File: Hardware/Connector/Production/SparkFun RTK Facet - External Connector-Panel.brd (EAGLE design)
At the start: 231.2 x 149 mm, 826 parts, among them J1 FPC_12_0.5MM_BACKFLIP, J103 FPC_12_0.5MM_BACKFLIP, J104 FPC_12_0.5MM_BACKFLIP, J105 Qwiic, J106 u-blox USB, J111 FPC_12_0.5MM_BACKFLIP, J112 FPC_12_0.5MM_BACKFLIP, J113 Qwiic, J114 u-blox USB, J119 FPC_12_0.5MM_BACKFLIP, J120 FPC_12_0.5MM_BACKFLIP, J121 Qwiic, J122 u-blox USB, J127 FPC_12_0.5MM_BACKFLIP, J128 FPC_12_0.5MM_BACKFLIP, J129 Qwiic, J130 u-blox USB, J135 FPC_12_0.5MM_BACKFLIP, J136 FPC_12_0.5MM_BACKFLIP, J137 Qwiic, J138 u-blox USB, J143 FPC_12_0.5MM_BACKFLIP, J144 FPC_12_0.5MM_BACKFLIP, J145 Qwiic, J146 u-blox USB, J15 FPC_12_0.5MM_BACKFLIP, J151 FPC_12_0.5MM_BACKFLIP, J152 FPC_12_0.5MM_BACKFLIP, J153 Qwiic, J154 u-blox USB, J159 FPC_12_0.5MM_BACKFLIP, J16 FPC_12_0.5MM_BACKFLIP, J160 FPC_12_0.5MM_BACKFLIP, J17 Qwiic, J18 u-blox USB, J23 FPC_12_0.5MM_BACKFLIP, J24 FPC_12_0.5MM_BACKFLIP, J25 Qwiic, J26 u-blox USB, J3 Qwiic, J31 FPC_12_0.5MM_BACKFLIP, J32 FPC_12_0.5MM_BACKFLIP, J33 Qwiic, J34 u-blox USB, J39 FPC_12_0.5MM_BACKFLIP, J4 Qwiic, J40 FPC_12_0.5MM_BACKFLIP, J41 Qwiic, J42 u-blox USB, J47 FPC_12_0.5MM_BACKFLIP, J48 FPC_12_0.5MM_BACKFLIP, J49 Qwiic, J5 u-blox USB, J50 u-blox USB, J55 FPC_12_0.5MM_BACKFLIP, J56 FPC_12_0.5MM_BACKFLIP, J57 Qwiic, J58 u-blox USB, J6 FPC_12_0.5MM_BACKFLIP, J63 FPC_12_0.5MM_BACKFLIP, J64 FPC_12_0.5MM_BACKFLIP, J65 Qwiic, J66 u-blox USB, J7 u-blox USB, J71 FPC_12_0.5MM_BACKFLIP, J72 FPC_12_0.5MM_BACKFLIP, J73 Qwiic, J74 u-blox USB, J79 FPC_12_0.5MM_BACKFLIP, J80 FPC_12_0.5MM_BACKFLIP, J81 Qwiic, J82 u-blox USB, J87 FPC_12_0.5MM_BACKFLIP, J88 FPC_12_0.5MM_BACKFLIP, J89 Qwiic, J90 u-blox USB, J95 FPC_12_0.5MM_BACKFLIP, J96 FPC_12_0.5MM_BACKFLIP, J97 Qwiic, J98 u-blox USB

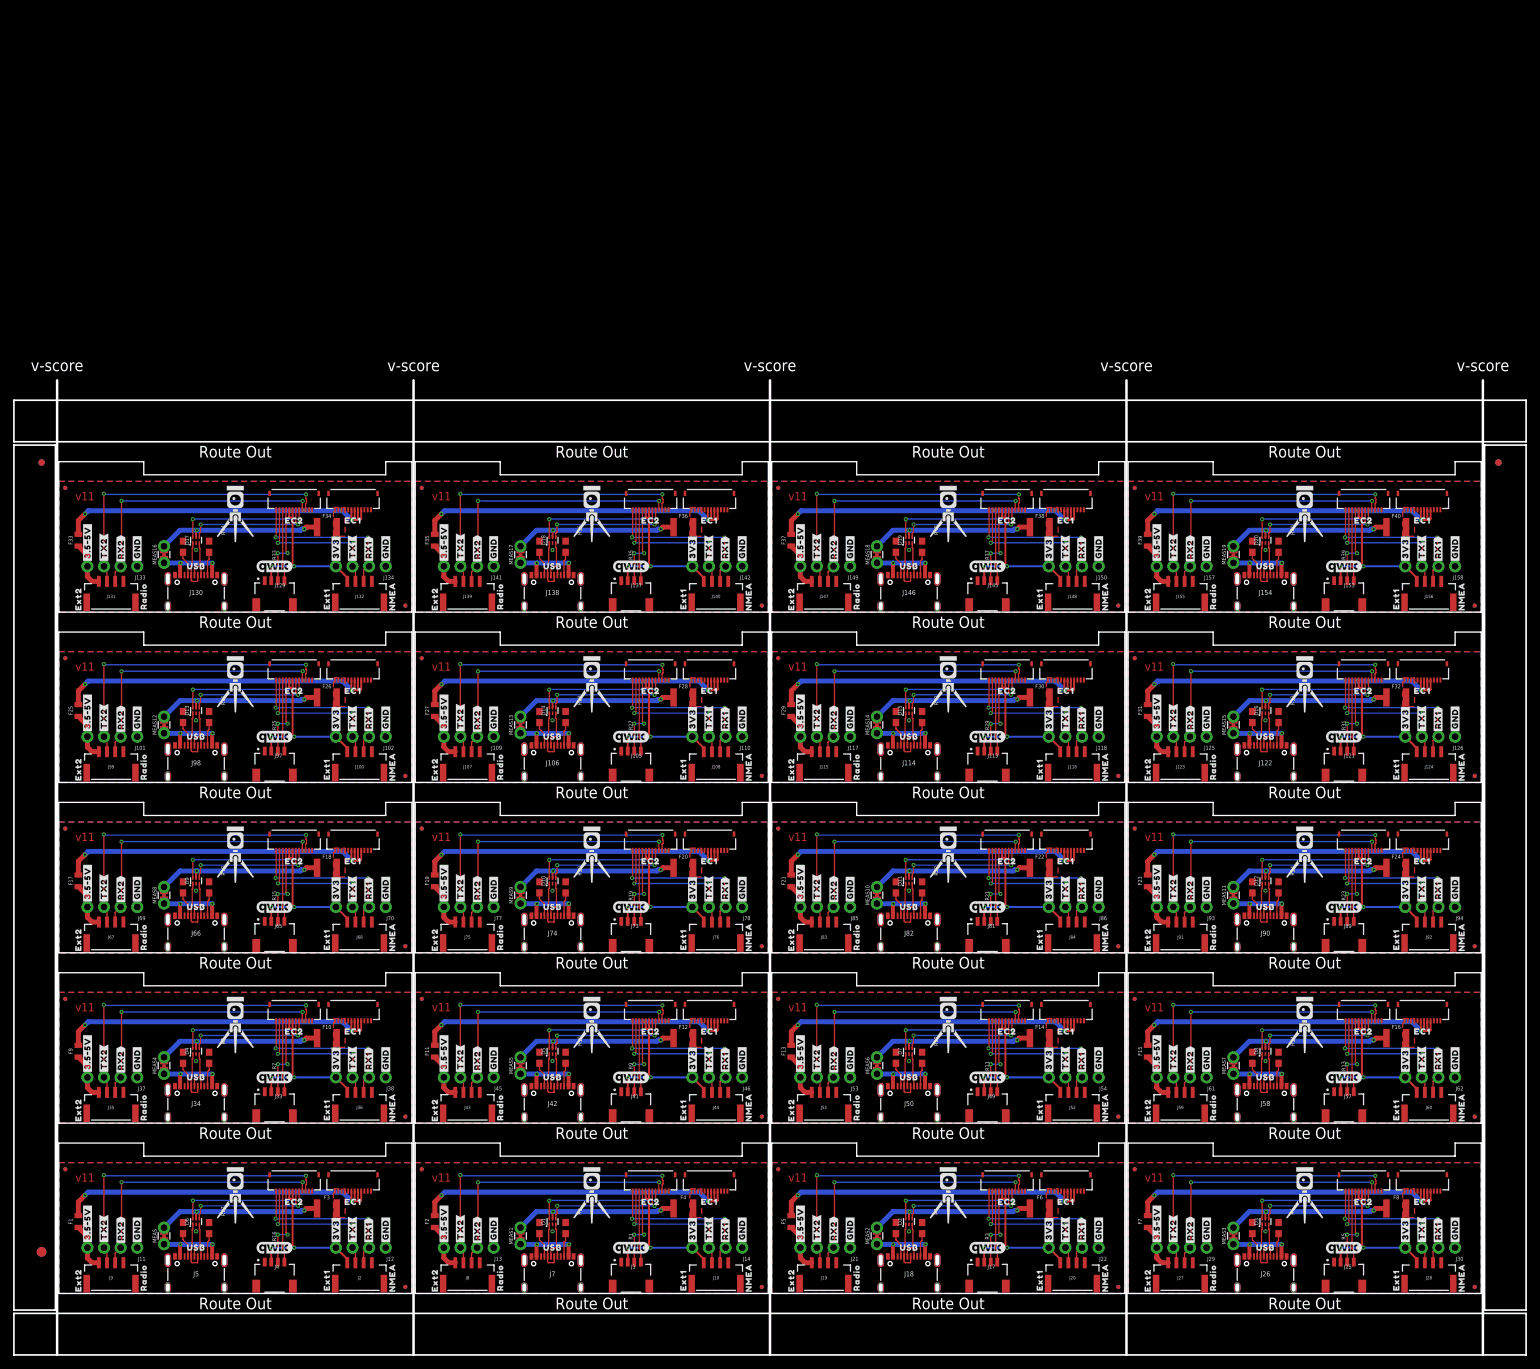
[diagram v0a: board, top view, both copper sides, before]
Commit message: Change connector panel orientation.
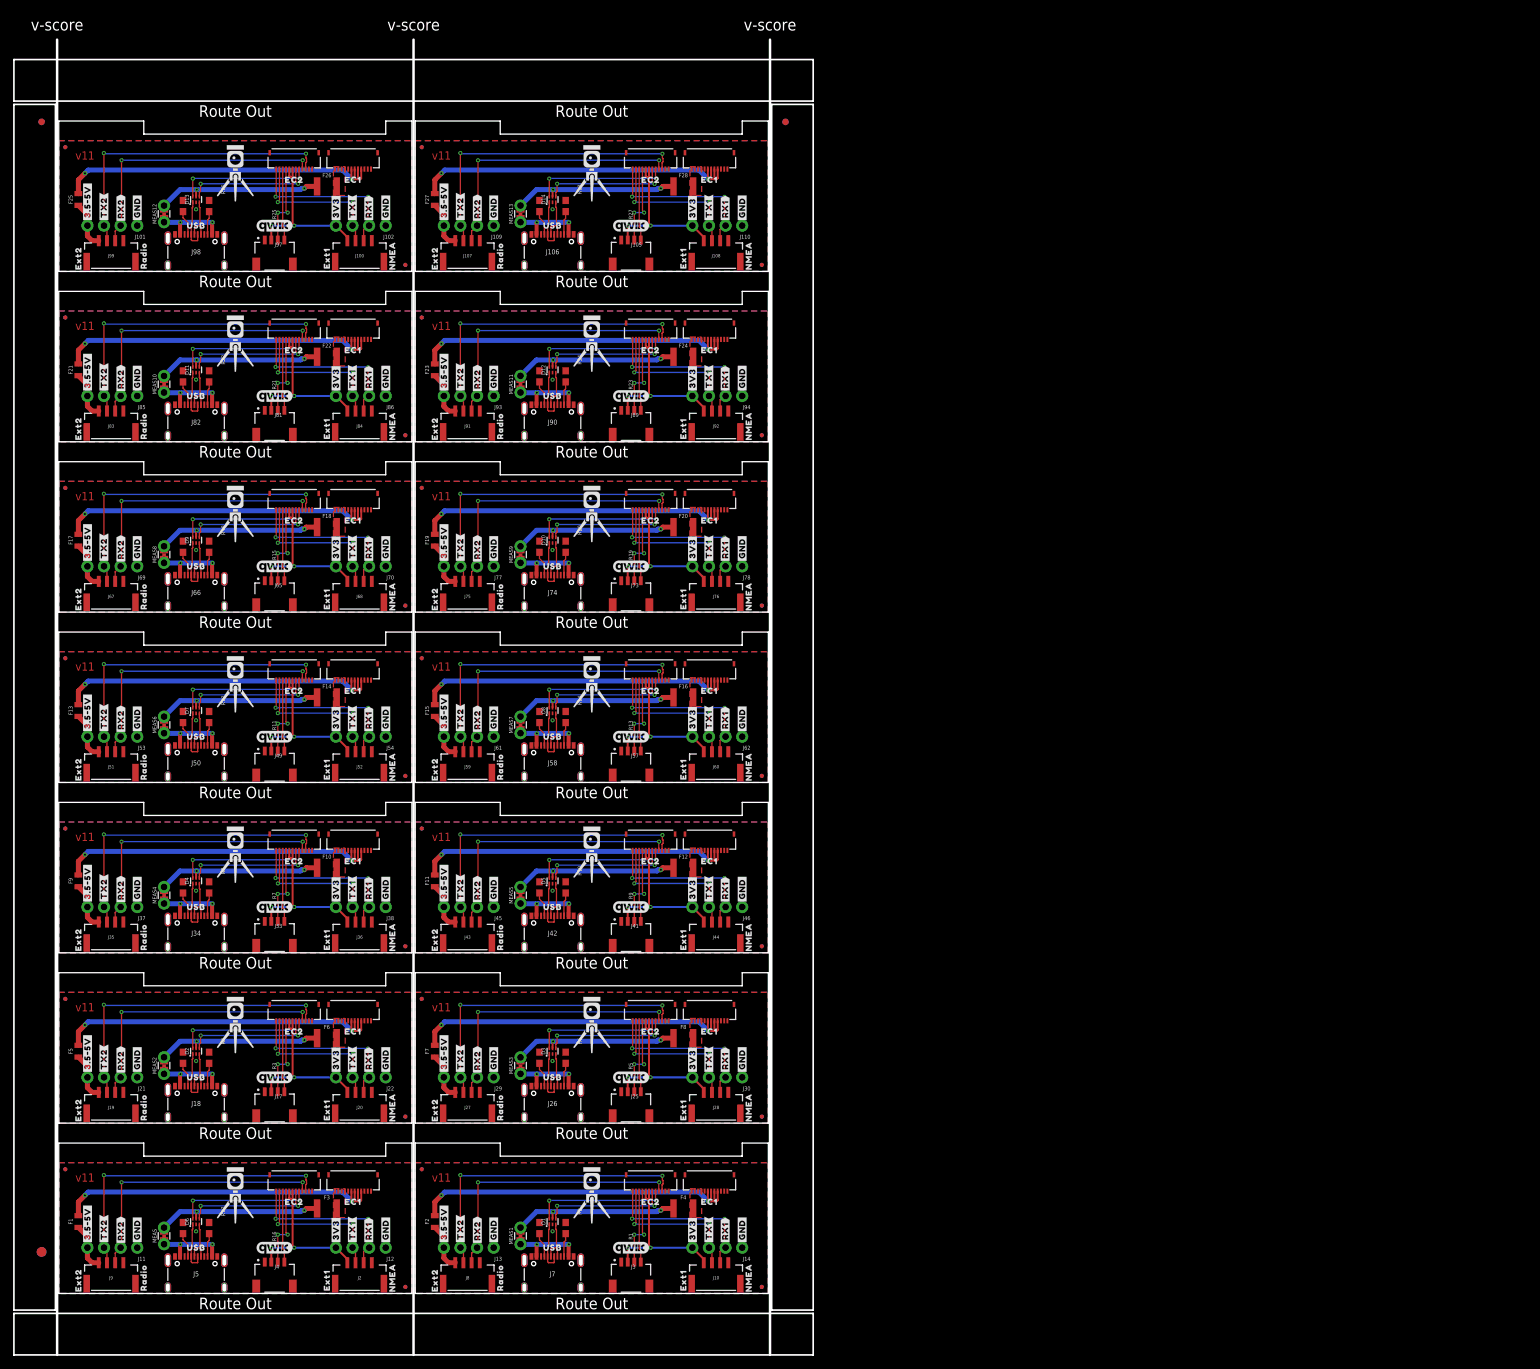
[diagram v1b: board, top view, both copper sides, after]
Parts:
- removed D15, D16, D17, D18, D19, D20: PRTR5V0U2F, SparkFun-IC-Power:SOT886
- removed F29, F31, F33, F35, F37, F39: 6V 0.5A, SparkFun-Fuses:0805
- removed F30, F32, F34, F36, F38, F40: 6V/2A, SparkFun-Fuses:1210
- removed J113, J121, J129, J137, J145, J153: Qwiic, SparkFun-Connectors:JST04_1MM_RA
- removed J114, J122, J130, J138, J146, J154: u-blox USB, SparkFun-Connectors:USB-C-16P-2LAYER-PADS
- removed J115, J116, J123, J124, J131, J132, J139, J140, J147, J148, J155, J156: (no value), SparkFun-Connectors:JST-4-SMD-1.25MM-LOCKING
- removed J117, J118, J125, J126, J133, J134, J141, J142, J149, J150, J157, J158: (no value), SparkFun-Connectors:1X04_NO_SILK
- removed J119, J120, J127, J128, J135, J136, J143, J144, J151, J152, J159, J160: FPC_12_0.5MM_BACKFLIP, RTK Facet:FPC_12_DOUBLESIDED_BACKFLIP
- removed JP54, JP55, JP56, JP57, JP58, JP59, JP60, JP62, JP63, JP64, JP65, JP66, JP67, JP68, JP69, JP70, JP72, JP73, JP74, JP75, JP76, JP77, JP78, JP79: FIDUCIALUFIDUCIAL, SparkFun-Aesthetics:FIDUCIAL-MICRO
- removed LOGO43, LOGO46, LOGO49, LOGO52, LOGO55, LOGO58: OSHW-LOGOMINI, SparkFun-Aesthetics:OSHW-LOGO-MINI
- removed LOGO44, LOGO47, LOGO50, LOGO53, LOGO56, LOGO59: SFE_LOGO_NAME_FLAME.1_INCH, SparkFun-Aesthetics:SFE_LOGO_NAME_FLAME_.1
- removed LOGO45, LOGO48, LOGO51, LOGO54, LOGO57, LOGO60: QWIIC_LOGO_CONNECTOR, SparkFun-Aesthetics:QWIIC_5.5MM
- removed MEAS14, MEAS15, MEAS16, MEAS17, MEAS18, MEAS19: (no value), SparkFun-Jumpers:COMBO-JUMPER_2_NC_TRACE
- removed R29, R30, R31, R32, R33, R34, R35, R36, R37, R38, R39, R40: 5.1k, SparkFun-Resistors:0603
- removed U$281, U$301, U$321, U$341, U$361, U$381: (no value), output:#RX2#2
- removed U$282, U$302, U$322, U$342, U$362, U$382: (no value), output:#TX2#1
- removed U$283, U$288, U$303, U$308, U$323, U$328, U$343, U$348, U$363, U$368, U$383, U$388: (no value), output:#GND#0
- removed U$284, U$304, U$324, U$344, U$364, U$384: (no value), output:#3#5#5V#0
- removed U$285, U$305, U$325, U$345, U$365, U$385: (no value), output:#3V3#0
- removed U$286, U$306, U$326, U$346, U$366, U$386: (no value), output:#TX1#1
- removed U$287, U$307, U$327, U$347, U$367, U$387: (no value), output:#RX1#2
- removed U$289, U$309, U$329, U$349, U$369, U$389: (no value), output:CONNECTORS1
- removed U$290, U$310, U$330, U$350, U$370, U$390: (no value), output:EXTERNAL0
- removed U$291, U$311, U$331, U$351, U$371, U$391: (no value), output:EC10
- removed U$292, U$312, U$332, U$352, U$372, U$392: (no value), output:EC21
- removed U$293, U$313, U$333, U$353, U$373, U$393: (no value), output:USB0
- removed U$294, U$314, U$334, U$354, U$374, U$394: (no value), output:EXT10
- removed U$295, U$315, U$335, U$355, U$375, U$395: (no value), output:EXT22
- removed U$296, U$316, U$336, U$356, U$376, U$396: (no value), output:NMEA1
- removed U$297, U$317, U$337, U$357, U$377, U$397: (no value), output:RADIO3
- removed U$298, U$299, U$318, U$319, U$338, U$339, U$358, U$359, U$378, U$379, U$398, U$399: (no value), output:RTK5#SVG0
- removed U$300, U$320, U$340, U$360, U$380, U$400: (no value), output:RTK_FACET0
- moved D11 134.1 mm to (21.0, 141.2)
- moved D12 134.1 mm to (75.5, 141.2)
- moved F21 134.1 mm to (3.00, 141.2)
- moved F22 134.1 mm to (41.0, 143.2)
- moved F23 134.1 mm to (57.5, 141.2)
- moved F24 134.1 mm to (95.5, 143.2)
- moved J81 134.1 mm to (33.0, 135.0)
- moved J82 134.1 mm to (21.0, 136.2)
- moved J83 134.1 mm to (8.00, 131.6)
- moved J84 134.1 mm to (46.0, 131.6)
- moved J85 134.1 mm to (12.0, 137.2)
- moved J86 134.1 mm to (50.0, 137.2)
- moved J87 134.1 mm to (45.0, 147.2)
- moved J88 134.1 mm to (36.0, 147.2)
- moved J89 134.1 mm to (87.5, 135.0)
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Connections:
- removed net 3.3V14: J113.2, J116.1, J118.4, J120.7, J120.8
- removed net 3.3V15: J121.2, J124.1, J126.4, J128.7, J128.8
- removed net 3.3V16: J129.2, J132.1, J134.4, J136.7, J136.8
- removed net 3.3V17: J137.2, J140.1, J142.4, J144.7, J144.8
- removed net 3.3V18: J145.2, J148.1, J150.4, J152.7, J152.8
- removed net 3.3V19: J153.2, J156.1, J158.4, J160.7, J160.8
- removed net CC29: J114.A5, R30.2
- removed net CC30: J114.B5, R29.2
- removed net CC31: J122.A5, R32.2
- removed net CC32: J122.B5, R31.2
- removed net CC33: J130.A5, R34.2
- removed net CC34: J130.B5, R33.2
- removed net CC35: J138.A5, R36.2
- removed net CC36: J138.B5, R35.2
- removed net CC37: J146.A5, R38.2
- removed net CC38: J146.B5, R37.2
- removed net CC39: J154.A5, R40.2
- removed net CC40: J154.B5, R39.2
- removed net ESP_21/SDA14: J113.3, J120.9
- removed net ESP_21/SDA15: J121.3, J128.9
- removed net ESP_21/SDA16: J129.3, J136.9
- removed net ESP_21/SDA17: J137.3, J144.9
- removed net ESP_21/SDA18: J145.3, J152.9
- removed net ESP_21/SDA19: J153.3, J160.9
- removed net ESP_22/SCL14: J113.4, J120.10
- removed net ESP_22/SCL15: J121.4, J128.10
- removed net ESP_22/SCL16: J129.4, J136.10
- removed net ESP_22/SCL17: J137.4, J144.10
- removed net ESP_22/SCL18: J145.4, J152.10
- removed net ESP_22/SCL19: J153.4, J160.10
- removed net EXTERNAL_SERIAL1_RXI14: J116.3, J118.2, J120.12
- removed net EXTERNAL_SERIAL1_RXI15: J124.3, J126.2, J128.12
- removed net EXTERNAL_SERIAL1_RXI16: J132.3, J134.2, J136.12
- removed net EXTERNAL_SERIAL1_RXI17: J140.3, J142.2, J144.12
- removed net EXTERNAL_SERIAL1_RXI18: J148.3, J150.2, J152.12
- removed net EXTERNAL_SERIAL1_RXI19: J156.3, J158.2, J160.12
- removed net EXTERNAL_SERIAL1_TXO14: J116.2, J118.3, J120.11
- removed net EXTERNAL_SERIAL1_TXO15: J124.2, J126.3, J128.11
- removed net EXTERNAL_SERIAL1_TXO16: J132.2, J134.3, J136.11
- removed net EXTERNAL_SERIAL1_TXO17: J140.2, J142.3, J144.11
- removed net EXTERNAL_SERIAL1_TXO18: J148.2, J150.3, J152.11
- removed net EXTERNAL_SERIAL1_TXO19: J156.2, J158.3, J160.11
- removed net GND14: D15.2, J113.1, J114.GND, J114.GND2, J114.SHLD1, J114.SHLD2, J114.SHLD3, J114.SHLD4, J115.4, J116.4, J117.1, J118.1, J119.1, J119.2, J119.3, J120.1, J120.2, R29.1, R30.1
- removed net GND15: D16.2, J121.1, J122.GND, J122.GND2, J122.SHLD1, J122.SHLD2, J122.SHLD3, J122.SHLD4, J123.4, J124.4, J125.1, J126.1, J127.1, J127.2, J127.3, J128.1, J128.2, R31.1, R32.1
- removed net GND16: D17.2, J129.1, J130.GND, J130.GND2, J130.SHLD1, J130.SHLD2, J130.SHLD3, J130.SHLD4, J131.4, J132.4, J133.1, J134.1, J135.1, J135.2, J135.3, J136.1, J136.2, R33.1, R34.1
- removed net GND17: D18.2, J137.1, J138.GND, J138.GND2, J138.SHLD1, J138.SHLD2, J138.SHLD3, J138.SHLD4, J139.4, J140.4, J141.1, J142.1, J143.1, J143.2, J143.3, J144.1, J144.2, R35.1, R36.1
- removed net GND18: D19.2, J145.1, J146.GND, J146.GND2, J146.SHLD1, J146.SHLD2, J146.SHLD3, J146.SHLD4, J147.4, J148.4, J149.1, J150.1, J151.1, J151.2, J151.3, J152.1, J152.2, R37.1, R38.1
- removed net GND19: D20.2, J153.1, J154.GND, J154.GND2, J154.SHLD1, J154.SHLD2, J154.SHLD3, J154.SHLD4, J155.4, J156.4, J157.1, J158.1, J159.1, J159.2, J159.3, J160.1, J160.2, R39.1, R40.1
- removed net N$15: F29.1, J115.1, J117.4
- removed net N$16: F31.1, J123.1, J125.4
- removed net N$17: F33.1, J131.1, J133.4
- removed net N$18: F35.1, J139.1, J141.4
- removed net N$19: F37.1, J147.1, J149.4
- removed net N$20: F39.1, J155.1, J157.4
- removed net USB1_D_M14: D15.1, J114.A7, J114.B7
- removed net USB1_D_M15: D16.1, J122.A7, J122.B7
- removed net USB1_D_M16: D17.1, J130.A7, J130.B7
- removed net USB1_D_M17: D18.1, J138.A7, J138.B7
- removed net USB1_D_M18: D19.1, J146.A7, J146.B7
- removed net USB1_D_M19: D20.1, J154.A7, J154.B7
- removed net USB1_D_P14: D15.3, J114.A6, J114.B6
- removed net USB1_D_P15: D16.3, J122.A6, J122.B6
- removed net USB1_D_P16: D17.3, J130.A6, J130.B6
- removed net USB1_D_P17: D18.3, J138.A6, J138.B6
- removed net USB1_D_P18: D19.3, J146.A6, J146.B6
- removed net USB1_D_P19: D20.3, J154.A6, J154.B6
- removed net USB_DM14: D15.6, J120.5
- removed net USB_DM15: D16.6, J128.5
- removed net USB_DM16: D17.6, J136.5
- removed net USB_DM17: D18.6, J144.5
- removed net USB_DM18: D19.6, J152.5
- removed net USB_DM19: D20.6, J160.5
- removed net USB_DP14: D15.4, J120.6
- removed net USB_DP15: D16.4, J128.6
- removed net USB_DP16: D17.4, J136.6
- removed net USB_DP17: D18.4, J144.6
- removed net USB_DP18: D19.4, J152.6
- removed net USB_DP19: D20.4, J160.6
- removed net VIN28: J114.VBUS1, J114.VBUS2, MEAS14.1, MEAS14.3
- removed net VIN29: D15.5, F30.1, MEAS14.2, MEAS14.4
- removed net VIN30: J122.VBUS1, J122.VBUS2, MEAS15.1, MEAS15.3
- removed net VIN31: D16.5, F32.1, MEAS15.2, MEAS15.4
- removed net VIN32: J130.VBUS1, J130.VBUS2, MEAS16.1, MEAS16.3
- removed net VIN33: D17.5, F34.1, MEAS16.2, MEAS16.4
- removed net VIN34: J138.VBUS1, J138.VBUS2, MEAS17.1, MEAS17.3
- removed net VIN35: D18.5, F36.1, MEAS17.2, MEAS17.4
- removed net VIN36: J146.VBUS1, J146.VBUS2, MEAS18.1, MEAS18.3
- removed net VIN37: D19.5, F38.1, MEAS18.2, MEAS18.4
- removed net VIN38: J154.VBUS1, J154.VBUS2, MEAS19.1, MEAS19.3
- removed net VIN39: D20.5, F40.1, MEAS19.2, MEAS19.4
- removed net V_BATT14: F29.2, J119.4, J119.5, J119.6, J119.7
- removed net V_BATT15: F31.2, J127.4, J127.5, J127.6, J127.7
- removed net V_BATT16: F33.2, J135.4, J135.5, J135.6, J135.7
- removed net V_BATT17: F35.2, J143.4, J143.5, J143.6, J143.7
- removed net V_BATT18: F37.2, J151.4, J151.5, J151.6, J151.7
- removed net V_BATT19: F39.2, J159.4, J159.5, J159.6, J159.7
- removed net V_USB14: F30.2, J119.10, J119.11, J119.12, J119.9
- removed net V_USB15: F32.2, J127.10, J127.11, J127.12, J127.9
- removed net V_USB16: F34.2, J135.10, J135.11, J135.12, J135.9
- removed net V_USB17: F36.2, J143.10, J143.11, J143.12, J143.9
- removed net V_USB18: F38.2, J151.10, J151.11, J151.12, J151.9
- removed net V_USB19: F40.2, J159.10, J159.11, J159.12, J159.9
- removed net ZED-RXI15: J115.3, J117.2, J120.4
- removed net ZED-RXI16: J123.3, J125.2, J128.4
- removed net ZED-RXI17: J131.3, J133.2, J136.4
- removed net ZED-RXI18: J139.3, J141.2, J144.4
- removed net ZED-RXI19: J147.3, J149.2, J152.4
- removed net ZED-RXI20: J155.3, J157.2, J160.4
- removed net ZED-TXO15: J115.2, J117.3, J120.3
- removed net ZED-TXO16: J123.2, J125.3, J128.3
- removed net ZED-TXO17: J131.2, J133.3, J136.3
- removed net ZED-TXO18: J139.2, J141.3, J144.3
- removed net ZED-TXO19: J147.2, J149.3, J152.3
- removed net ZED-TXO20: J155.2, J157.3, J160.3
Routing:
- net V_BATT14: track 52.7 -> 0.00 mm, vias 2 -> 0
- net V_BATT17: track 52.7 -> 0.00 mm, vias 2 -> 0
- net V_BATT18: track 52.7 -> 0.00 mm, vias 2 -> 0
- net V_BATT16: track 52.7 -> 0.00 mm, vias 2 -> 0
- net V_BATT15: track 52.7 -> 0.00 mm, vias 2 -> 0
- net V_BATT19: track 52.7 -> 0.00 mm, vias 2 -> 0
- net ZED-TXO19: track 47.0 -> 0.00 mm, vias 2 -> 0
- net ZED-TXO20: track 47.0 -> 0.00 mm, vias 2 -> 0
- net ZED-TXO15: track 47.0 -> 0.00 mm, vias 2 -> 0
- net ZED-TXO16: track 47.0 -> 0.00 mm, vias 2 -> 0
- net ZED-TXO18: track 47.0 -> 0.00 mm, vias 2 -> 0
- net ZED-TXO17: track 47.0 -> 0.00 mm, vias 2 -> 0
- net ZED-RXI15: track 41.8 -> 0.00 mm, vias 2 -> 0
- net ZED-RXI18: track 41.8 -> 0.00 mm, vias 2 -> 0
- net ZED-RXI19: track 41.8 -> 0.00 mm, vias 2 -> 0
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- removed copper zone on layer 1, net GND14
- removed copper zone on layer 16, net GND14
- removed copper zone on layer 1, net GND15
- removed copper zone on layer 16, net GND15
- removed copper zone on layer 1, net GND16
- removed copper zone on layer 16, net GND16
- removed copper zone on layer 1, net GND17
- removed copper zone on layer 16, net GND17
- removed copper zone on layer 1, net GND18
- removed copper zone on layer 16, net GND18
- removed copper zone on layer 1, net GND19
- removed copper zone on layer 16, net GND19
- removed copper zone on layer 1, net V_USB14
- removed copper zone on layer 1, net V_USB15
- removed copper zone on layer 1, net V_USB16
- removed copper zone on layer 1, net V_USB17
- removed copper zone on layer 1, net V_USB18
- removed copper zone on layer 1, net V_USB19
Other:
- board size 231.2 x 149 mm -> 122.2 x 201.1 mm

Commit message: Reduce Main, Connector, Display, and Cell board widths by 1mm to allow for v-score protrusion.
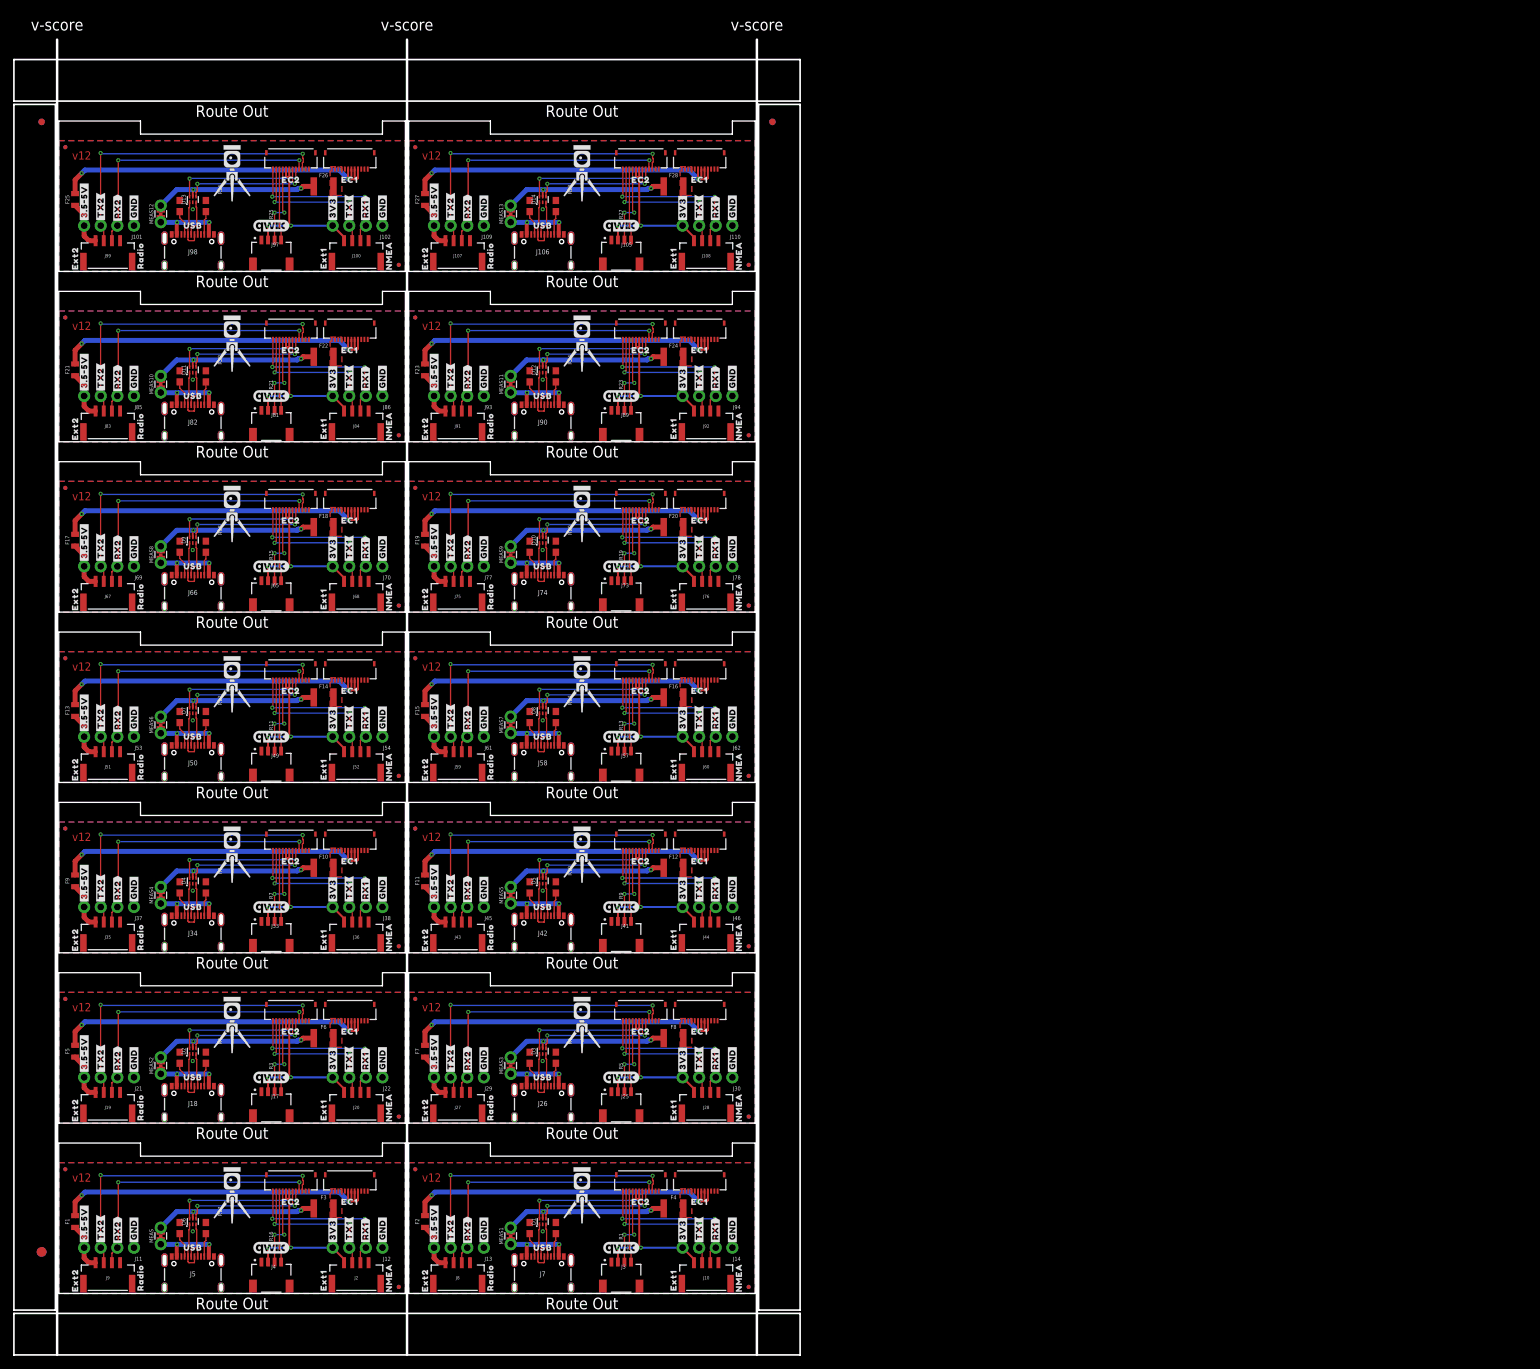
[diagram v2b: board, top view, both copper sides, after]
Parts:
- moved JP1 2.00 mm to (105.5, 1.00)
- moved JP11 2.00 mm to (105.5, 27.0)
- moved JP17 2.00 mm to (105.5, 53.1)
- moved JP19 2.00 mm to (105.5, 53.1)
- moved JP26 2.00 mm to (105.5, 79.1)
- moved JP28 2.00 mm to (105.5, 79.1)
- moved JP3 2.00 mm to (105.5, 1.00)
- moved JP34 2.00 mm to (105.5, 105.2)
- moved JP36 2.00 mm to (105.5, 105.2)
- moved JP42 2.00 mm to (105.5, 131.2)
- moved JP44 2.00 mm to (105.5, 131.2)
- moved JP50 2.00 mm to (105.5, 157.3)
- moved JP52 2.00 mm to (105.5, 157.3)
- moved JP9 2.00 mm to (105.5, 27.0)
- moved E$3 2.00 mm to (109.1, 179.2)
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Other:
- board size 122.2 x 201.1 mm -> 120.2 x 201.1 mm
- board text added: "v12"
- board text removed: "v11"
